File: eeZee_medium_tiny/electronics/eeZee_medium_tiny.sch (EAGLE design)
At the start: 11 parts, among them IC1 TINY24/44/84, J2 avrisp, Q1 16MHz

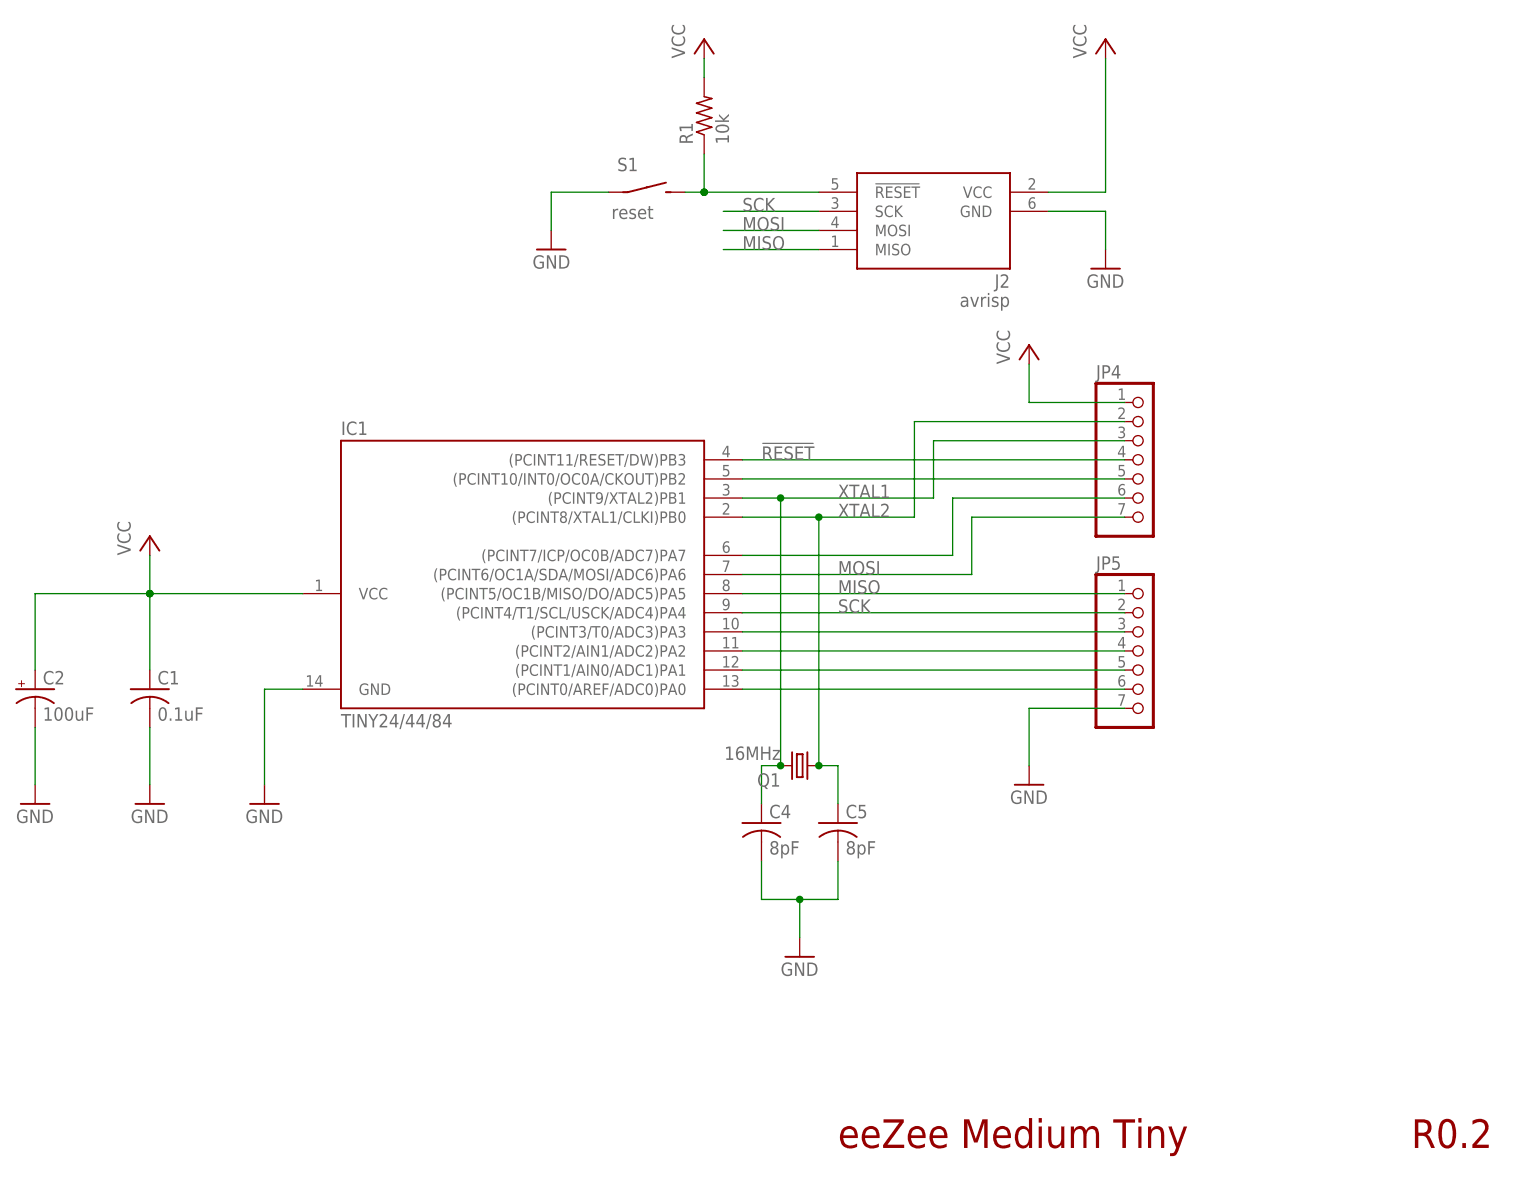
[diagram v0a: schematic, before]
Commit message: Revised pads for IC, revised 10uF filtering cap footprint to 1206.
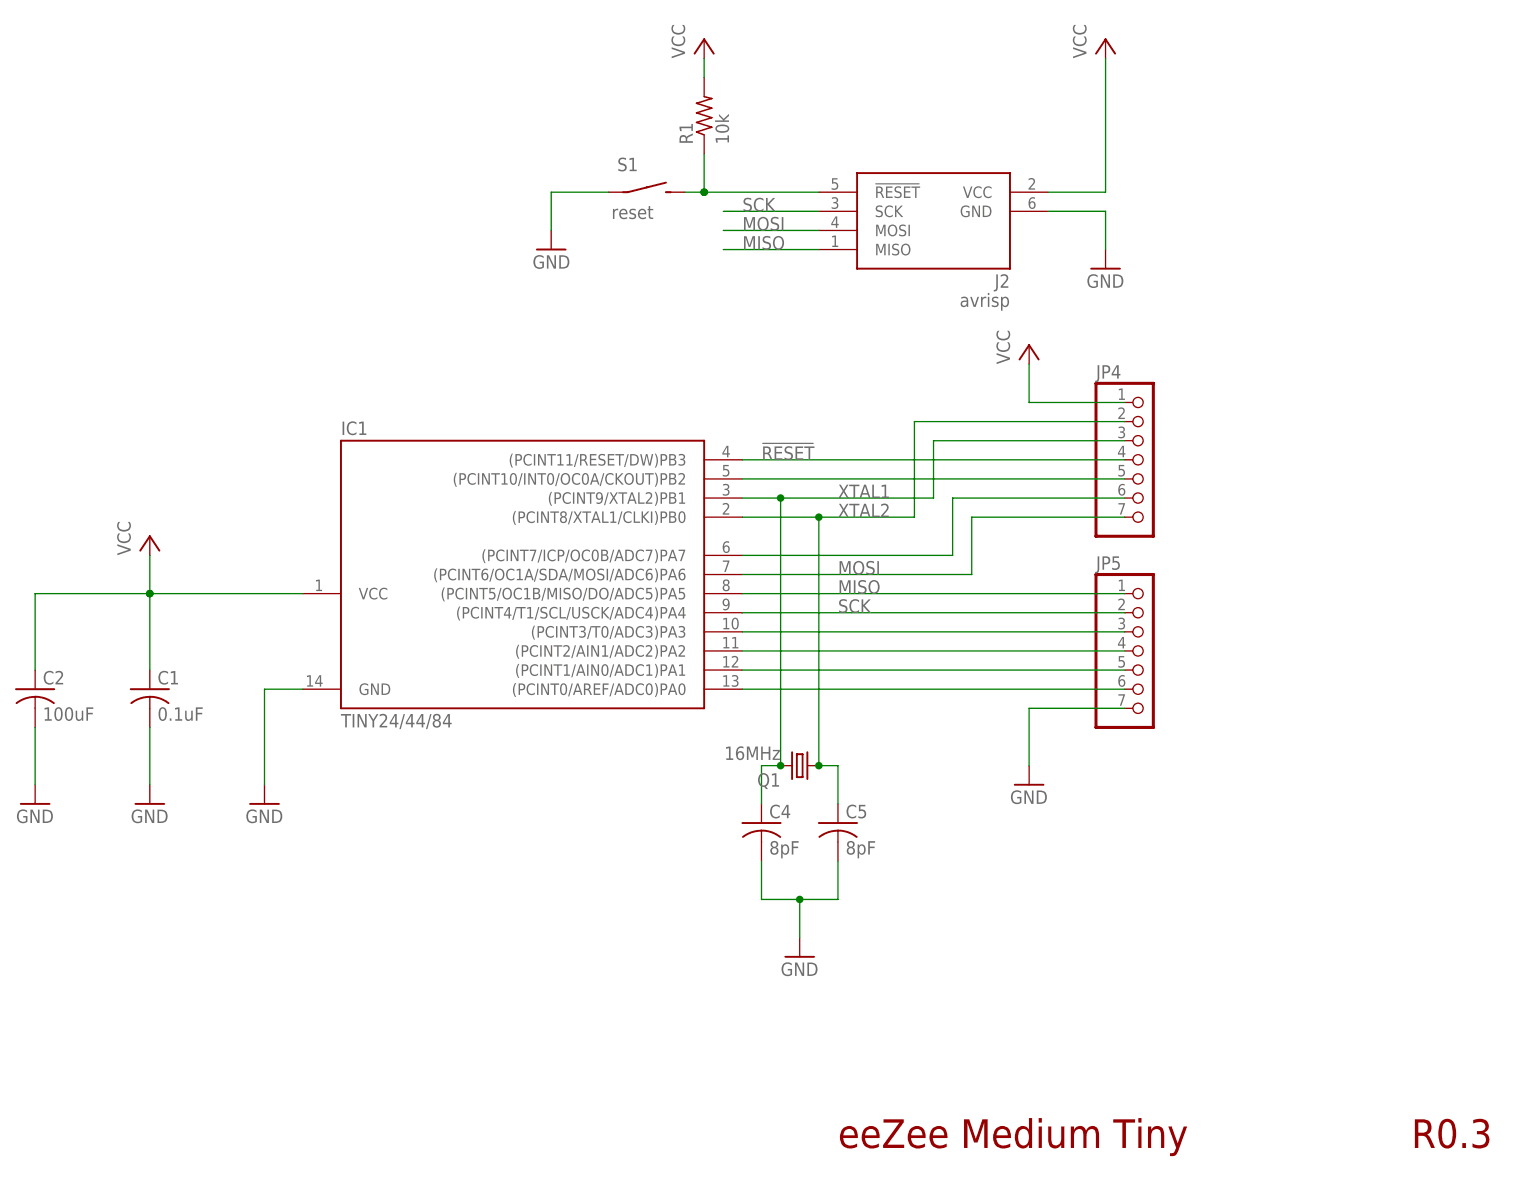
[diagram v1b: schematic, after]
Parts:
- C2: device mes_rcl:CAP_POL_SMC_B -> rcl:C-USC1206
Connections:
- net GND: now also C2.2; no longer C2.-
- net VCC: now also C2.1; no longer C2.+
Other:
- note added: "R0.3"
- note removed: "R0.2"
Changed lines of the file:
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@@
 <part name="GND5" library="supply1" deviceset="GND" device=""/>
 <part name="GND6" library="supply1" deviceset="GND" device=""/>
-<part name="C2" library="mes_rcl" deviceset="CAP_POL" device="_SMC_B" value="100uF">
+<part name="C2" library="rcl" deviceset="C-US" device="C1206" value="100uF">
 <attribute name="BOM" value="EXCLUDE"/>
 <attribute name="PARTNO" value="MCTT21X106M6R3CT"/>
@@
 <plain>
 <text x="154.94" y="22.86" size="3.81" layer="94">eeZee Medium Tiny</text>
-<text x="231.14" y="22.86" size="3.81" layer="94">R0.2</text>
+<text x="231.14" y="22.86" size="3.81" layer="94">R0.3</text>
 </plain>
 <instances>
@@
 <pinref part="GND6" gate="1" pin="GND"/>
 <wire x1="48.26" y1="78.74" x2="48.26" y2="71.12" width="0.1524" layer="91"/>
-<pinref part="C2" gate="G$1" pin="-"/>
+<pinref part="C2" gate="G$1" pin="2"/>
 </segment>
 <segment>
@@
 <wire x1="63.5" y1="96.52" x2="63.5" y2="101.6" width="0.1524" layer="91"/>
 <junction x="63.5" y="96.52"/>
-<pinref part="C2" gate="G$1" pin="+"/>
+<pinref part="C2" gate="G$1" pin="1"/>
 <pinref part="IC1" gate="1" pin="VCC"/>
 </segment>
